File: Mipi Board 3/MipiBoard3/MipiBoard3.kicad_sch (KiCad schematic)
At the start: 30 parts, among them J1 Power/Control Top, J2 Bank A Top, J3 Bank B Top, J4 MIPI1, J5 MIPI2, J6 Bank A Bottom, J7 Bank B Bottom, J8 Power/Control Bottom, U1 LM339, U2 LM339

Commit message: smallUpdate
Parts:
- added C3: C, symbol Device:C
- added R19, R20, R21, R22, R23, R24: R, Resistor_SMD:R_0402_1005Metric, symbol Device:R
- added U3: LM339, symbol Comparator:LM339
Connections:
- net +3V3: now also C3.1
- net 14_L14_SRCC_N/1.2C: now also U3.13
- net 14_L14_SRCC_P/1.2C: now also U3.14
- net 14_L17_N/1.2C: now also U1.13
- net 14_L17_P/1.2C: now also U1.14
- net 14_L7_N/1.2B: now also U2.14; no longer U1.2
- net 14_L9_N/1.2C: now also U1.1; no longer U1.13
- net 14_L9_P/1.2B: now also U1.2; no longer U1.1
- net 34_L1/1.5B_N: now also R22.2
- net 34_L3/1.5B_N: now also R24.2
- net 34_L5/1.5B_N: now also R23.2
- net 34_L7/1.5B_N: now also R19.2
- net 34_L8/1.5B_N: now also R20.2
- net 34_L9/1.5B_N: now also R21.2
- net 35_E6_SCL/1.4A: now also U3.1
- net 35_K5_SDA/1.4D: now also U3.2
- net DividerVoltage: now also U1.8 (-), U2.8 (-), U3.10 (-), U3.4 (-), U3.6 (-), U3.8 (-)
- net GND: now also U3.12 (V-)
- net at R12.1: now also U1.5 (+); no longer U2.11 (+)
- net at R18.1: now also U3.11 (+); no longer U1.11 (+)
- net at U1.9 (+): now also R22.1
- net at R17.1: now also U3.5 (+); no longer U1.7 (+)
- net at R9.1: now also U2.11 (+); no longer U2.7 (+)
- net at R16.1: now also U1.11 (+); no longer U1.5 (+)
- net at U2.9 (+): now also R20.1
- new net: R23.1, U3.7 (+)
- new net: R21.1, U1.7 (+)
- new net: R19.1, U2.7 (+)
- new net: R24.1, U3.9 (+)
- new net: C3.2, U3.3 (V+)
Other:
- moved on the sheet: C2, R10, R11, R12, R13, R16, R17, R18, R7, R8, R9, U1A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

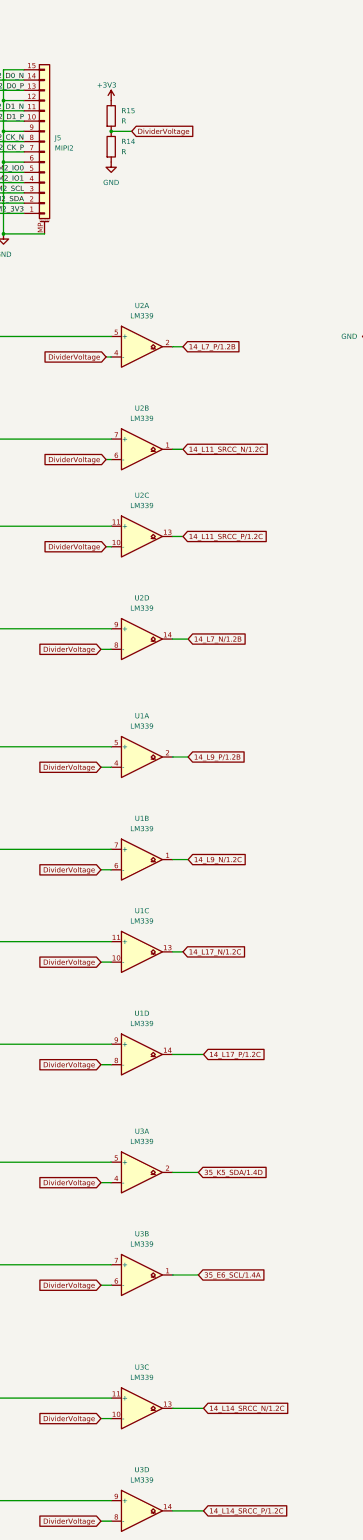
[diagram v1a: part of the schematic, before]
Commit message: adding pull ups
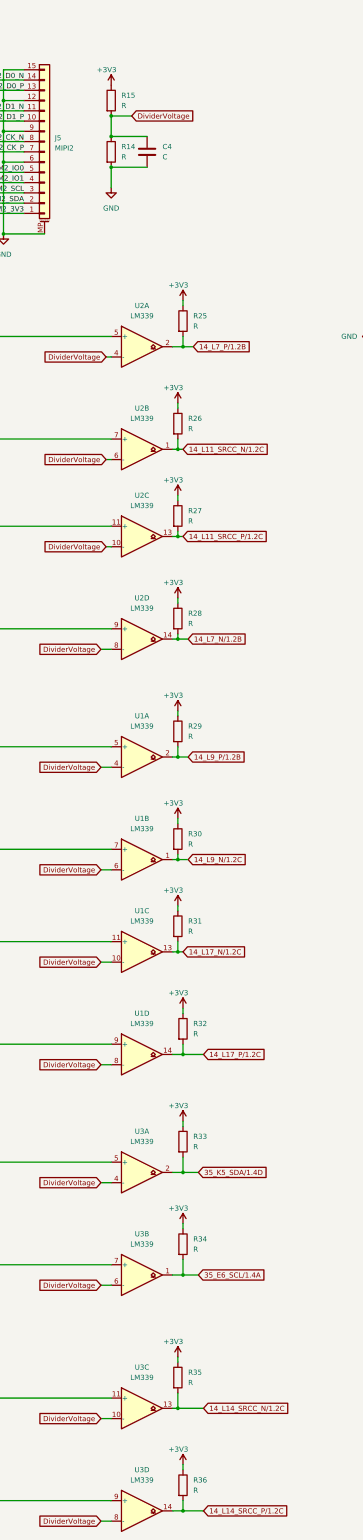
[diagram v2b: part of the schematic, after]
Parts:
- added C4: C, symbol Device:C
- added R25, R26, R27, R28, R29, R30, R31, R32, R33, R34, R35, R36: R, Resistor_SMD:R_0402_1005Metric, symbol Device:R
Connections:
- net +3V3: now also R25.1, R26.1, R27.1, R28.1, R29.1, R30.1, R31.1, R32.1, R33.1, R34.1, R35.1, R36.1
- net 14_L11_SRCC_N/1.2C: now also R26.2
- net 14_L11_SRCC_P/1.2C: now also R27.2
- net 14_L14_SRCC_N/1.2C: now also R35.2
- net 14_L14_SRCC_P/1.2C: now also R36.2
- net 14_L17_N/1.2C: now also R31.2
- net 14_L17_P/1.2C: now also R32.2
- net 14_L7_N/1.2B: now also R28.2
- net 14_L7_P/1.2B: now also R25.2
- net 14_L9_N/1.2C: now also R30.2
- net 14_L9_P/1.2B: now also R29.2
- net 35_E6_SCL/1.4A: now also R34.2
- net 35_K5_SDA/1.4D: now also R33.2
- net DividerVoltage: now also C4.2
- net GND: now also C4.1
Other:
- moved on the sheet: R14, R15

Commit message: Components layedout
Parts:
- removed unit 2 of U3
- removed unit 1 of U3
- added unit 1 of U2
- added unit 2 of U2
- C1, C2, C3, C4: footprint (none) -> Capacitor_SMD:C_0201_0603Metric
- R14, R15: footprint Resistor_SMD:R_0805_2012Metric -> Resistor_SMD:R_0603_1608Metric
- R25, R26, R27, R28, R29, R30, R31, R32, R33, R34, R35, R36: footprint Resistor_SMD:R_0402_1005Metric -> Resistor_SMD:R_0603_1608Metric
- U1, U2, U3: footprint (none) -> Package_SO:TSSOP-14-1EP_4.4x5mm_P0.65mm
- U3: renamed from U2; footprint (none) -> Package_SO:TSSOP-14-1EP_4.4x5mm_P0.65mm
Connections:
- net +3V3: now also C1.2, C2.2, U1.3 (V+), U2.3 (V+), U3.3 (V+); no longer C1.1, C2.1
- net 14_L11_SRCC_N/1.2C: now also U3.14; no longer U3.1
- net 14_L14_SRCC_N/1.2C: now also U3.1; no longer U3.13
- net 14_L14_SRCC_P/1.2C: now also U3.2; no longer U3.14
- net 14_L17_N/1.2C: now also U1.1; no longer U1.13
- net 14_L17_P/1.2C: now also U1.2; no longer U1.14
- net 14_L7_P/1.2B: now also U3.13; no longer U3.2
- net 14_L9_N/1.2C: now also U1.14; no longer U1.1
- net 14_L9_P/1.2B: now also U1.13; no longer U1.2
- net 35_E6_SCL/1.4A: now also U2.2
- net 35_K5_SDA/1.4D: now also U2.1
- net DividerVoltage: now also U1.10 (-), U1.4 (-), U1.6 (-), U1.8 (-), U3.10 (-), U3.4 (-), U3.6 (-), U3.8 (-), U2.4 (-), U2.6 (-); no longer U1.10 (-), U1.4 (-), U1.6 (-), U1.8 (-), U3.10 (-), U3.4 (-), U3.6 (-), U3.8 (-)
- net GND: now also C1.1, C2.1, C3.2
- net at R23.1: now also U2.5 (+)
- net at R17.1: now also U2.7 (+)
- net at R12.1: now also U1.11 (+); no longer U1.5 (+)
- net at R18.1: now also U3.7 (+); no longer U3.11 (+)
- net at R16.1: now also U1.7 (+); no longer U1.11 (+)
- net at R22.1: now also U1.5 (+); no longer U1.9 (+)
- net at R21.1: now also U1.9 (+); no longer U1.7 (+)
- net at R19.1: now also U3.9 (+); no longer U3.7 (+)
- net at R24.1: now also U3.5 (+); no longer U3.9 (+)
- net at R6.1: now also U3.11 (+); no longer U3.5 (+)
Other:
- moved on the sheet: C1, C2, C3, U1E, U3E

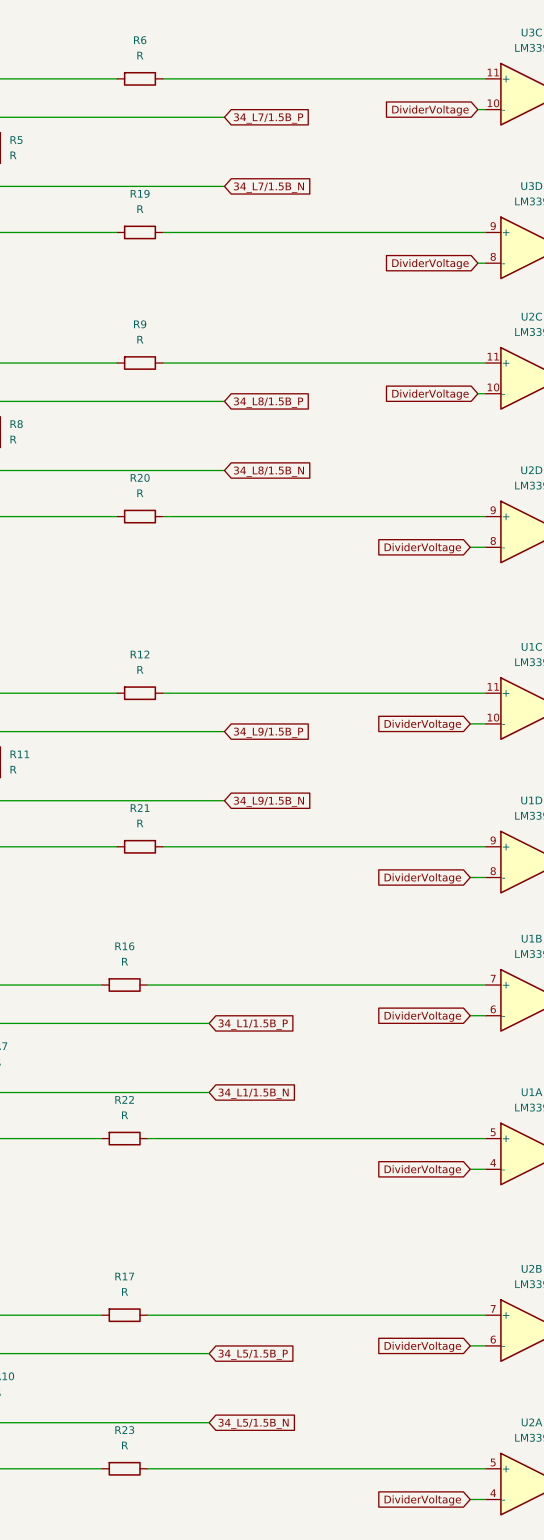
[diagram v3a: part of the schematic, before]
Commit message: first few wires routed
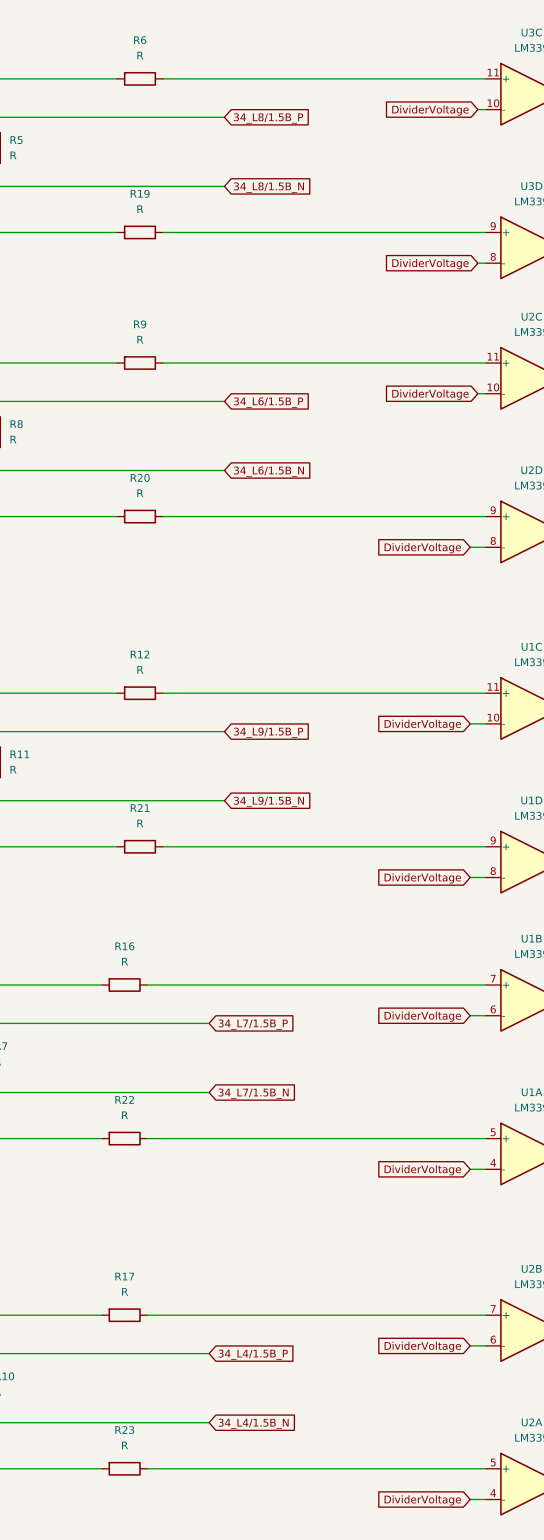
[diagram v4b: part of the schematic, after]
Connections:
- net 34_L1/1.5B_N is gone; now on net 34_L7/1.5B_N: J4.14 (Pin_14), R22.2, R7.2
- net 34_L1/1.5B_P is gone; now on net 34_L7/1.5B_P: J4.13 (Pin_13), R16.2, R7.1
- net 34_L4/1.5B_N: now also J4.11 (Pin_11), R10.2, R23.2
- net 34_L4/1.5B_P: now also J4.10 (Pin_10), R10.1, R17.2
- net 34_L5/1.5B_N: no longer J4.11 (Pin_11), R10.2, R23.2
- net 34_L5/1.5B_P: no longer J4.10 (Pin_10), R10.1, R17.2
- net 34_L6/1.5B_N: now also J5.11 (Pin_11), R20.2, R8.2
- net 34_L6/1.5B_P: now also J5.10 (Pin_10), R8.1, R9.2
- net 34_L7/1.5B_N: no longer J5.14 (Pin_14), R19.2, R5.2
- net 34_L7/1.5B_P: no longer J5.13 (Pin_13), R5.1, R6.2
- net 34_L8/1.5B_N: now also J5.14 (Pin_14), R19.2, R5.2; no longer J5.11 (Pin_11), R20.2, R8.2
- net 34_L8/1.5B_P: now also J5.13 (Pin_13), R5.1, R6.2; no longer J5.10 (Pin_10), R8.1, R9.2
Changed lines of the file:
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@@
 		)
 	)
-	(global_label "34_L7{slash}1.5B_N"
-		(shape input)
-		(at 359.41 113.03 0)
-		(fields_autoplaced yes)
-		(effects
-			(font
-				(size 1.27 1.27)
-			)
-			(justify left)
-		)
-		(property "Intersheetrefs" "${INTERSHEET_REFS}"
-			(at 375.9418 113.03 0)
-			(hide yes)
-			(show_name no)
-			(do_not_autoplace no)
-			(effects
-				(font
-					(size 1.27 1.27)
-				)
-				(justify left)
-			)
-		)
-	)
 	(global_label "14_L17_N{slash}1.2C"
 		(shape input)
@@
 		)
 	)
+	(global_label "34_L8{slash}1.5B_P"
+		(shape input)
+		(at 359.41 101.6 0)
+		(fields_autoplaced yes)
+		(effects
+			(font
+				(size 1.27 1.27)
+			)
+			(justify left)
+		)
+		(property "Intersheetrefs" "${INTERSHEET_REFS}"
+			(at 375.8813 101.6 0)
+			(hide yes)
+			(show_name no)
+			(do_not_autoplace no)
+			(effects
+				(font
+					(size 1.27 1.27)
+				)
+				(justify left)
+			)
+		)
+	)
 	(global_label "14_L24_P{slash}1.2D"
 		(shape input)
@@
 		)
 	)
+	(global_label "34_L6{slash}1.5B_N"
+		(shape input)
+		(at 359.41 160.02 0)
+		(fields_autoplaced yes)
+		(effects
+			(font
+				(size 1.27 1.27)
+			)
+			(justify left)
+		)
+		(property "Intersheetrefs" "${INTERSHEET_REFS}"
+			(at 375.9418 160.02 0)
+			(hide yes)
+			(show_name no)
+			(do_not_autoplace no)
+			(effects
+				(font
+					(size 1.27 1.27)
+				)
+				(justify left)
+			)
+		)
+	)
 	(global_label "TDO{slash}6.4B"
 		(shape input)
@@
 		)
 	)
-	(global_label "Cam2_CK_N"
+	(global_label "34_L7{slash}1.5B_N"
 		(shape input)
-		(at 368.3 46.99 180)
+		(at 356.87 262.89 0)
 		(fields_autoplaced yes)
 		(effects
@@
 				(size 1.27 1.27)
 			)
-			(justify right)
+			(justify left)
 		)
 		(property "Intersheetrefs" "${INTERSHEET_REFS}"
-			(at 354.1873 46.99 0)
+			(at 373.4018 262.89 0)
 			(hide yes)
 			(show_name no)
@@
 					(size 1.27 1.27)
 				)
-				(justify right)
+				(justify left)
 			)
 		)
 	)
-	(global_label "34_L8{slash}1.5B_P"
+	(global_label "Cam2_CK_N"
 		(shape input)
-		(at 226.06 236.22 0)
+		(at 368.3 46.99 180)
 		(fields_autoplaced yes)
 		(effects
@@
 				(size 1.27 1.27)
 			)
-			(justify left)
+			(justify right)
 		)
 		(property "Intersheetrefs" "${INTERSHEET_REFS}"
-			(at 242.5313 236.22 0)
+			(at 354.1873 46.99 0)
 			(hide yes)
 			(show_name no)
@@
 					(size 1.27 1.27)
 				)
-				(justify left)
+				(justify right)
 			)
 		)
 	)
-	(global_label "34_L7{slash}1.5B_P"
+	(global_label "34_L8{slash}1.5B_P"
 		(shape input)
-		(at 359.41 101.6 0)
+		(at 226.06 236.22 0)
 		(fields_autoplaced yes)
 		(effects
@@
 		)
 		(property "Intersheetrefs" "${INTERSHEET_REFS}"
-			(at 375.8813 101.6 0)
+			(at 242.5313 236.22 0)
 			(hide yes)
 			(show_name no)
@@
 		)
 	)
-	(global_label "34_L8{slash}1.5B_P"
-		(shape input)
-		(at 359.41 148.59 0)
-		(fields_autoplaced yes)
-		(effects
-			(font
-				(size 1.27 1.27)
-			)
-			(justify left)
-		)
-		(property "Intersheetrefs" "${INTERSHEET_REFS}"
-			(at 375.8813 148.59 0)
-			(hide yes)
-			(show_name no)
-			(do_not_autoplace no)
-			(effects
-				(font
-					(size 1.27 1.27)
-				)
-				(justify left)
-			)
-		)
-	)
 	(global_label "34_L5{slash}1.5B_N"
 		(shape input)
@@
 		)
 	)
+	(global_label "34_L7{slash}1.5B_P"
+		(shape input)
+		(at 356.87 251.46 0)
+		(fields_autoplaced yes)
+		(effects
+			(font
+				(size 1.27 1.27)
+			)
+			(justify left)
+		)
+		(property "Intersheetrefs" "${INTERSHEET_REFS}"
+			(at 373.3413 251.46 0)
+			(hide yes)
+			(show_name no)
+			(do_not_autoplace no)
+			(effects
+				(font
+					(size 1.27 1.27)
+				)
+				(justify left)
+			)
+		)
+	)
+	(global_label "34_L4{slash}1.5B_N"
+		(shape input)
+		(at 356.87 317.5 0)
+		(fields_autoplaced yes)
+		(effects
+			(font
+				(size 1.27 1.27)
+			)
+			(justify left)
+		)
+		(property "Intersheetrefs" "${INTERSHEET_REFS}"
+			(at 373.4018 317.5 0)
+			(hide yes)
+			(show_name no)
+			(do_not_autoplace no)
+			(effects
+				(font
+					(size 1.27 1.27)
+				)
+				(justify left)
+			)
+		)
+	)
 	(global_label "LED1{slash}1.5D"
 		(shape input)
@@
 		)
 	)
-	(global_label "34_L1{slash}1.5B_N"
+	(global_label "14_L21_P{slash}1.2D"
 		(shape input)
-		(at 356.87 262.89 0)
+		(at 203.2 160.02 180)
 		(fields_autoplaced yes)
 		(effects
@@
 				(size 1.27 1.27)
 			)
-			(justify left)
+			(justify right)
 		)
 		(property "Intersheetrefs" "${INTERSHEET_REFS}"
-			(at 373.4018 262.89 0)
+			(at 185.5192 160.02 0)
 			(hide yes)
 			(show_name no)
@@
 					(size 1.27 1.27)
 				)
-				(justify left)
+				(justify right)
 			)
 		)
 	)
-	(global_label "14_L21_P{slash}1.2D"
+	(global_label "DividerVoltage"
 		(shape input)
-		(at 203.2 160.02 180)
+		(at 400.05 275.59 180)
 		(fields_autoplaced yes)
 		(effects
@@
 		)
 		(property "Intersheetrefs" "${INTERSHEET_REFS}"
-			(at 185.5192 160.02 0)
+			(at 383.5787 275.59 0)
 			(hide yes)
 			(show_name no)
@@
 		)
 	)
-	(global_label "DividerVoltage"
+	(global_label "34_L6{slash}1.5B_P"
 		(shape input)
-		(at 400.05 275.59 180)
+		(at 359.41 148.59 0)
 		(fields_autoplaced yes)
 		(effects
@@
 				(size 1.27 1.27)
 			)
-			(justify right)
+			(justify left)
 		)
 		(property "Intersheetrefs" "${INTERSHEET_REFS}"
-			(at 383.5787 275.59 0)
+			(at 375.8813 148.59 0)
 			(hide yes)
 			(show_name no)
@@
 					(size 1.27 1.27)
 				)
-				(justify right)
+				(justify left)
 			)
 		)
@@
 		)
 	)
-	(global_label "34_L5{slash}1.5B_P"
-		(shape input)
-		(at 356.87 306.07 0)
-		(fields_autoplaced yes)
-		(effects
-			(font
-				(size 1.27 1.27)
-			)
-			(justify left)
-		)
-		(property "Intersheetrefs" "${INTERSHEET_REFS}"
-			(at 373.3413 306.07 0)
-			(hide yes)
-			(show_name no)
-			(do_not_autoplace no)
-			(effects
-				(font
-					(size 1.27 1.27)
-				)
-				(justify left)
-			)
-		)
-	)
 	(global_label "35_L13_MRCC_P{slash}1.4C"
 		(shape input)
@@
 		)
 	)
-	(global_label "34_L8{slash}1.5B_N"
-		(shape input)
-		(at 359.41 160.02 0)
-		(fields_autoplaced yes)
-		(effects
-			(font
-				(size 1.27 1.27)
-			)
-			(justify left)
-		)
-		(property "Intersheetrefs" "${INTERSHEET_REFS}"
-			(at 375.9418 160.02 0)
-			(hide yes)
-			(show_name no)
-			(do_not_autoplace no)
-			(effects
-				(font
-					(size 1.27 1.27)
-				)
-				(justify left)
-			)
-		)
-	)
 	(global_label "34_L9{slash}1.5B_N"
 		(shape input)
@@
 		)
 	)
-	(global_label "34_L1{slash}1.5B_P"
-		(shape input)
-		(at 356.87 251.46 0)
-		(fields_autoplaced yes)
-		(effects
-			(font
-				(size 1.27 1.27)
-			)
-			(justify left)
-		)
-		(property "Intersheetrefs" "${INTERSHEET_REFS}"
-			(at 373.3413 251.46 0)
-			(hide yes)
-			(show_name no)
-			(do_not_autoplace no)
-			(effects
-				(font
-					(size 1.27 1.27)
-				)
-				(justify left)
-			)
-		)
-	)
 	(global_label "14_L10_N{slash}1.2C"
 		(shape input)
@@
 		)
 	)
-	(global_label "34_L5{slash}1.5B_N"
-		(shape input)
-		(at 356.87 317.5 0)
-		(fields_autoplaced yes)
-		(effects
-			(font
-				(size 1.27 1.27)
-			)
-			(justify left)
-		)
-		(property "Intersheetrefs" "${INTERSHEET_REFS}"
-			(at 373.4018 317.5 0)
-			(hide yes)
-			(show_name no)
-			(do_not_autoplace no)
-			(effects
-				(font
-					(size 1.27 1.27)
-				)
-				(justify left)
-			)
-		)
-	)
 	(global_label "35_L14_SRCC_N{slash}1.4C"
 		(shape input)
@@
 		)
 	)
+	(global_label "34_L8{slash}1.5B_N"
+		(shape input)
+		(at 359.41 113.03 0)
+		(fields_autoplaced yes)
+		(effects
+			(font
+				(size 1.27 1.27)
+			)
+			(justify left)
+		)
+		(property "Intersheetrefs" "${INTERSHEET_REFS}"
+			(at 375.9418 113.03 0)
+			(hide yes)
+			(show_name no)
+			(do_not_autoplace no)
+			(effects
+				(font
+					(size 1.27 1.27)
+				)
+				(justify left)
+			)
+		)
+	)
 	(global_label "35_L21_N{slash}1.4D"
 		(shape input)
@@
 			)
 		)
+	)
+	(global_label "34_L4{slash}1.5B_P"
+		(shape input)
+		(at 356.87 306.07 0)
+		(fields_autoplaced yes)
+		(effects
+			(font
+				(size 1.27 1.27)
+			)
+			(justify left)
+		)
+		(property "Intersheetrefs" "${INTERSHEET_REFS}"
+			(at 373.3413 306.07 0)
+			(hide yes)
+			(show_name no)
+			(do_not_autoplace no)
+			(effects
+				(font
+					(size 1.27 1.27)
+				)
+				(justify left)
+			)
+		)

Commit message: Finished wiring
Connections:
- net 14_L10_N/1.2C: no longer J5.3 (Pin_3), R3.1
- net 14_L10_P/1.2C: no longer J5.2 (Pin_2), R4.1
- net 14_L11_SRCC_N/1.2C: now also R28.2, U2.14; no longer R26.2, U3.14
- net 14_L14_SRCC_N/1.2C: now also J5.4 (Pin_4); no longer R35.2, U3.1
- net 14_L14_SRCC_P/1.2C: now also J5.5 (Pin_5); no longer R36.2, U3.2
- net 14_L15_N/1.2C: now also R34.2, U2.2; no longer J4.3 (Pin_3), R1.1
- net 14_L15_P/1.2C: now also R33.2, U2.1; no longer J4.2 (Pin_2), R2.1
- net 14_L16_N/1.2C: no longer J5.5 (Pin_5)
- net 14_L16_P/1.2C: no longer J5.4 (Pin_4)
- net 14_L17_N/1.2C: now also J4.4 (Pin_4); no longer R31.2, U1.1
- net 14_L17_P/1.2C: now also J4.5 (Pin_5); no longer R32.2, U1.2
- net 14_L21_N/1.2D: now also J4.2 (Pin_2), R2.1
- net 14_L21_P/1.2D: now also J4.3 (Pin_3), R1.1
- net 14_L22_N/1.2D: now also R36.2, U3.2; no longer J4.5 (Pin_5)
- net 14_L22_P/1.2D: now also R35.2, U3.1; no longer J4.4 (Pin_4)
- net 14_L7_N/1.2B: now also R30.2, U1.14; no longer R28.2, U2.14
- net 14_L7_P/1.2B: now also R29.2, U1.13; no longer R25.2, U3.13
- net 14_L9_N/1.2C: now also R32.2, U1.2; no longer R30.2, U1.14
- net 14_L9_P/1.2B: now also R31.2, U1.1; no longer R29.2, U1.13
- net 35_E6_SCL/1.4A: now also J5.3 (Pin_3), R3.1; no longer R34.2, U2.2
- net 35_K5_SDA/1.4D: now also J5.2 (Pin_2), R4.1; no longer R33.2, U2.1
- net D10_1V35/7.1B: now also R25.2, U3.13
- net D9_1V35/7.1B: now also R26.2, U3.14
